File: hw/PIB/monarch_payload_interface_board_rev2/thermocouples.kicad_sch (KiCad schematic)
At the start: 30 parts, among them U3 MAX31856MUD_T, U5 MAX31856MUD_T, U6 MAX31856MUD_T, U7 MAX31856MUD_T, U8 MAX31856MUD_T

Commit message: AD7124 Fixes
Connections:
- net *FAULT: now reaches U3.13 (~{FAULT})
- net *DRDY: now reaches U3.7 (~{DRDY})
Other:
- moved on the sheet: C24, C25
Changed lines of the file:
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@@
 	)
 	(junction
-		(at 86.36 78.74)
-		(diameter 0)
-		(color 0 0 0 0)
-	)
-	(junction
-		(at 86.36 81.28)
+		(at 88.9 81.28)
 		(diameter 0)
 		(color 0 0 0 0)
@@
 	)
 	(junction
-		(at 90.17 78.74)
+		(at 92.71 78.74)
 		(diameter 0)
 		(color 0 0 0 0)
@@
 	)
 	(junction
+		(at 88.9 78.74)
+		(diameter 0)
+		(color 0 0 0 0)
+	)
+	(junction
 		(at 210.82 34.29)
 		(diameter 0)
@@
 	(wire
 		(pts
-			(xy 86.36 82.55) (xy 86.36 81.28)
+			(xy 88.9 82.55) (xy 88.9 81.28)
 		)
 		(stroke
@@
 	(wire
 		(pts
-			(xy 90.17 78.74) (xy 91.44 78.74)
-		)
-		(stroke
-			(width 0)
-			(type default)
-		)
-	)
-	(wire
-		(pts
 			(xy 128.27 88.9) (xy 127 88.9)
 		)
@@
 	(wire
 		(pts
+			(xy 73.66 78.74) (xy 88.9 78.74)
+		)
+		(stroke
+			(width 0)
+			(type default)
+		)
+	)
+	(wire
+		(pts
 			(xy 110.49 41.91) (xy 116.84 41.91)
 		)
@@
 	(wire
 		(pts
-			(xy 86.36 88.9) (xy 86.36 87.63)
+			(xy 88.9 88.9) (xy 88.9 87.63)
 		)
 		(stroke
@@
 	(wire
 		(pts
-			(xy 73.66 78.74) (xy 86.36 78.74)
+			(xy 38.1 36.83) (xy 36.83 36.83)
 		)
 		(stroke
@@
 	(wire
 		(pts
-			(xy 38.1 36.83) (xy 36.83 36.83)
+			(xy 73.66 96.52) (xy 77.47 96.52)
 		)
 		(stroke
@@
 	(wire
 		(pts
-			(xy 73.66 96.52) (xy 77.47 96.52)
+			(xy 38.1 39.37) (xy 36.83 39.37)
 		)
 		(stroke
@@
 	(wire
 		(pts
-			(xy 38.1 39.37) (xy 36.83 39.37)
+			(xy 207.01 52.07) (xy 207.01 41.91)
 		)
 		(stroke
@@
 	(wire
 		(pts
-			(xy 207.01 52.07) (xy 207.01 41.91)
+			(xy 20.32 91.44) (xy 26.67 91.44)
 		)
 		(stroke
@@
 	(wire
 		(pts
-			(xy 20.32 91.44) (xy 26.67 91.44)
+			(xy 128.27 86.36) (xy 127 86.36)
 		)
 		(stroke
@@
 	(wire
 		(pts
-			(xy 128.27 86.36) (xy 127 86.36)
+			(xy 73.66 81.28) (xy 88.9 81.28)
 		)
 		(stroke
@@
 	(wire
 		(pts
-			(xy 86.36 71.12) (xy 86.36 73.66)
+			(xy 88.9 71.12) (xy 88.9 73.66)
 		)
 		(stroke
@@
 	(wire
 		(pts
-			(xy 90.17 78.74) (xy 90.17 81.28)
+			(xy 92.71 78.74) (xy 92.71 81.28)
 		)
 		(stroke
@@
 	(wire
 		(pts
-			(xy 73.66 81.28) (xy 86.36 81.28)
-		)
-		(stroke
-			(width 0)
-			(type default)
-		)
-	)
-	(wire
-		(pts
-			(xy 86.36 78.74) (xy 90.17 78.74)
+			(xy 88.9 78.74) (xy 93.98 78.74)
 		)
 		(stroke
@@
 	(wire
 		(pts
-			(xy 90.17 81.28) (xy 86.36 81.28)
+			(xy 92.71 81.28) (xy 88.9 81.28)
 		)
 		(stroke
@@
 		)
 	)
+	(hierarchical_label "*FAULT"
+		(shape input)
+		(at 73.66 88.9 0)
+		(effects
+			(font
+				(size 1.27 1.27)
+			)
+			(justify left)
+		)
+	)
 	(hierarchical_label "SPI2_MOSI"
 		(shape input)
@@
 		)
 	)
+	(hierarchical_label "*DRDY"
+		(shape input)
+		(at 73.66 86.36 0)
+		(effects
+			(font
+				(size 1.27 1.27)
+			)
+			(justify left)
+		)
+	)
 	(symbol
 		(lib_id "power:GND")
@@
 	(symbol
 		(lib_id "power:GND")
-		(at 86.36 71.12 180)
+		(at 88.9 71.12 180)
 		(unit 1)
 		(body_style 1)
@@
 		(fields_autoplaced yes)
 		(property "Reference" "#PWR047"
-			(at 86.36 64.77 0)
+			(at 88.9 64.77 0)
 			(hide yes)
 			(show_name no)
@@
 		)
 		(property "Value" "GND"
-			(at 86.36 66.04 0)
+			(at 88.9 66.04 0)
 			(show_name no)
 			(do_not_autoplace no)
@@
 		)
 		(property "Footprint" ""
-			(at 86.36 71.12 0)
+			(at 88.9 71.12 0)
 			(hide yes)
 			(show_name no)
@@
 		)
 		(property "Datasheet" ""
-			(at 86.36 71.12 0)
+			(at 88.9 71.12 0)
 			(hide yes)
 			(show_name no)
@@
 		)
 		(property "Description" "Power symbol creates a global label with name \"GND\" , ground"
-			(at 86.36 71.12 0)
+			(at 88.9 71.12 0)
 			(hide yes)
 			(show_name no)
@@
 	(symbol
 		(lib_id "Device:C_Small")
-		(at 86.36 85.09 0)
+		(at 88.9 85.09 0)
 		(unit 1)
 		(body_style 1)
@@
 		(dnp no)
 		(property "Reference" "C25"
-			(at 79.502 84.074 0)
+			(at 82.042 84.074 0)
 			(show_name no)
 			(do_not_autoplace no)
@@
 		)
 		(property "Value" "0.1u"
-			(at 79.248 86.36 0)
+			(at 81.788 86.36 0)
 			(show_name no)
 			(do_not_autoplace no)
@@
 		)
 		(property "Footprint" "Capacitor_SMD:C_0603_1608Metric"
-			(at 86.36 85.09 0)
+			(at 88.9 85.09 0)
 			(hide yes)
 			(show_name no)
@@
 		)
 		(property "Datasheet" ""
-			(at 86.36 85.09 0)
+			(at 88.9 85.09 0)
 			(hide yes)
 			(show_name no)
@@
 		)
 		(property "Description" "Unpolarized capacitor, small symbol"
-			(at 86.36 85.09 0)
+			(at 88.9 85.09 0)
 			(hide yes)
 			(show_name no)
@@
 	(symbol
 		(lib_id "power:GND")
-		(at 86.36 88.9 0)
+		(at 88.9 88.9 0)
 		(unit 1)
 		(body_style 1)
@@
 		(dnp no)
 		(property "Reference" "#PWR048"
-			(at 86.36 95.25 0)
+			(at 88.9 95.25 0)
 			(hide yes)
 			(show_name no)
@@
 		)
 		(property "Value" "GND"
-			(at 89.916 91.186 0)
+			(at 92.456 91.186 0)
 			(show_name no)
 			(do_not_autoplace no)
@@
 		)
 		(property "Footprint" ""
-			(at 86.36 88.9 0)
+			(at 88.9 88.9 0)
 			(hide yes)
 			(show_name no)
@@
 		)
 		(property "Datasheet" ""
-			(at 86.36 88.9 0)
+			(at 88.9 88.9 0)
 			(hide yes)
 			(show_name no)
@@
 		)
 		(property "Description" "Power symbol creates a global label with name \"GND\" , ground"
-			(at 86.36 88.9 0)
+			(at 88.9 88.9 0)
 			(hide yes)
 			(show_name no)
@@
 	(symbol
 		(lib_id "power:+3V3")
-		(at 91.44 78.74 270)
+		(at 93.98 78.74 270)
 		(unit 1)
 		(body_style 1)
@@
 		(fields_autoplaced yes)
 		(property "Reference" "#PWR046"
-			(at 87.63 78.74 0)
+			(at 90.17 78.74 0)
 			(hide yes)
 			(show_name no)
@@
 		)
 		(property "Value" "+3V3"
-			(at 95.25 78.7399 90)
+			(at 97.79 78.7399 90)
 			(show_name no)
 			(do_not_autoplace no)
@@
 		)
 		(property "Footprint" ""
-			(at 91.44 78.74 0)
+			(at 93.98 78.74 0)
 			(hide yes)
 			(show_name no)
@@
 		)
 		(property "Datasheet" ""
-			(at 91.44 78.74 0)
+			(at 93.98 78.74 0)
 			(hide yes)
 			(show_name no)
@@
 		)
 		(property "Description" "Power symbol creates a global label with name \"+3V3\""
-			(at 91.44 78.74 0)
+			(at 93.98 78.74 0)
 			(hide yes)
 			(show_name no)
@@
 	(symbol
 		(lib_id "Device:C_Small")
-		(at 86.36 76.2 0)
+		(at 88.9 76.2 0)
 		(unit 1)
 		(body_style 1)
@@
 		(dnp no)
 		(property "Reference" "C24"
-			(at 77.724 74.676 0)
+			(at 80.264 74.676 0)
 			(show_name no)
 			(do_not_autoplace no)
@@
 		)
 		(property "Value" "0.01u"
-			(at 77.47 76.962 0)
+			(at 80.01 76.962 0)
 			(show_name no)
 			(do_not_autoplace no)
@@
 		)
 		(property "Footprint" "Capacitor_SMD:C_0603_1608Metric"
-			(at 86.36 76.2 0)
+			(at 88.9 76.2 0)
 			(hide yes)
 			(show_name no)
@@
 		)
 		(property "Datasheet" ""
-			(at 86.36 76.2 0)
+			(at 88.9 76.2 0)
 			(hide yes)
 			(show_name no)
@@
 		)
 		(property "Description" "Unpolarized capacitor, small symbol"
-			(at 86.36 76.2 0)
+			(at 88.9 76.2 0)
 			(hide yes)
 			(show_name no)

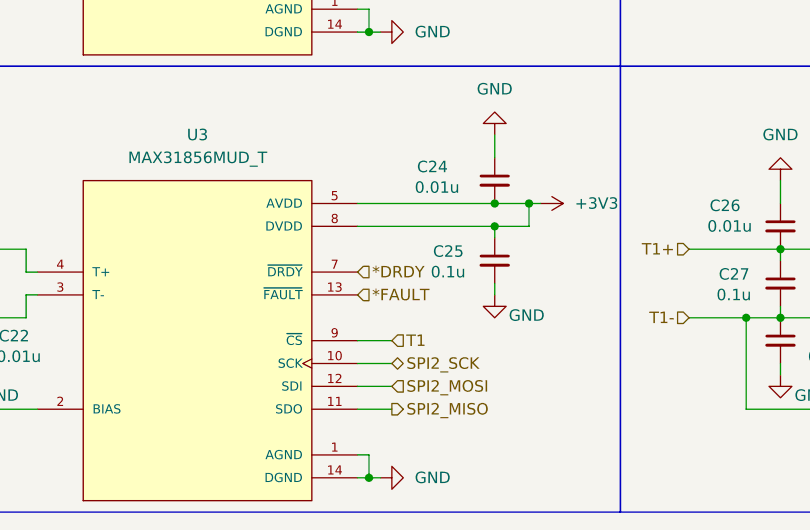
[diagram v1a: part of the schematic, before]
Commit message: Connector Footprints / Additions + Validated MAX31856
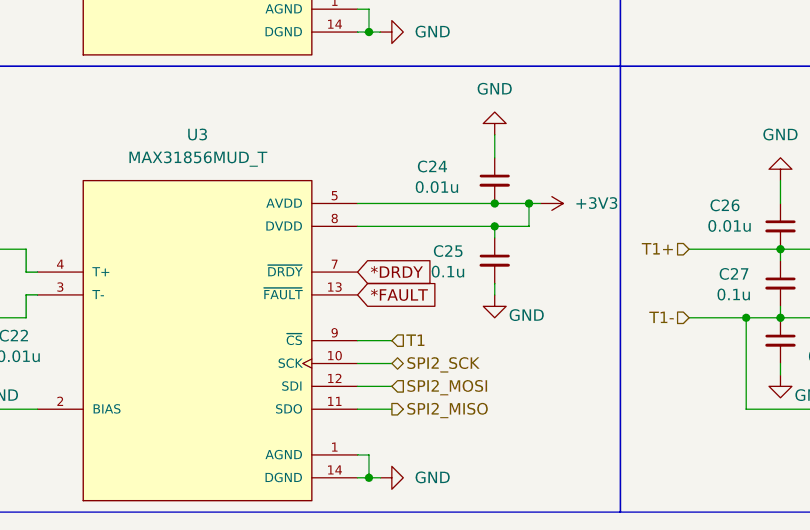
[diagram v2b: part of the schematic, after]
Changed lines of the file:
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@@
+		)
+	)
+	(global_label "*FAULT"
+		(shape input)
+		(at 73.66 88.9 0)
+		(fields_autoplaced yes)
+		(effects
+			(font
+				(size 1.27 1.27)
+			)
+			(justify left)
+		)
+		(property "Intersheetrefs" "${INTERSHEET_REFS}"
+			(at 82.462 88.9 0)
+			(hide yes)
+			(show_name no)
+			(do_not_autoplace no)
+			(effects
+				(font
+					(size 1.27 1.27)
+				)
+				(justify left)
+			)
+		)
+	)
+	(global_label "*DRDY"
+		(shape input)
+		(at 73.66 86.36 0)
+		(fields_autoplaced yes)
+		(effects
+			(font
+				(size 1.27 1.27)
+			)
+			(justify left)
+		)
+		(property "Intersheetrefs" "${INTERSHEET_REFS}"
+			(at 81.8572 86.36 0)
+			(hide yes)
+			(show_name no)
+			(do_not_autoplace no)
+			(effects
+				(font
+					(size 1.27 1.27)
+				)
+				(justify left)
+			)
 		)
 	)
@@
 		)
 	)
-	(hierarchical_label "*FAULT"
-		(shape input)
-		(at 73.66 88.9 0)
-		(effects
-			(font
-				(size 1.27 1.27)
-			)
-			(justify left)
-		)
-	)
 	(hierarchical_label "SPI2_MOSI"
 		(shape input)
@@
 		(effects
 			(font
-				(size 1.27 1.27)
-			)
-			(justify left)
-		)
-	)
-	(hierarchical_label "*DRDY"
-		(shape input)
-		(at 73.66 86.36 0)
-		(effects
-			(font

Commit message: Schematic Unconnected Fix
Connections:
- no-connect marks 0 -> 8
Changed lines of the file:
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@@
 		(color 0 0 0 0)
+	)
+	(no_connect
+		(at 163.83 39.37)
+	)
+	(no_connect
+		(at 73.66 36.83)
+	)
+	(no_connect
+		(at 163.83 88.9)
+	)
+	(no_connect
+		(at 254 36.83)
+	)
+	(no_connect
+		(at 254 39.37)
+	)
+	(no_connect
+		(at 163.83 86.36)
+	)
+	(no_connect
+		(at 163.83 36.83)
+	)
+	(no_connect
+		(at 73.66 39.37)
 	)
 	(wire
